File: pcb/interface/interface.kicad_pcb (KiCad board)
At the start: 2 copper layers, 45.8 x 24.8 mm, 15 parts, among them J1 SEGMENTS, J16 BUS_IN, J17 BUS_OUT, J5 SELECT, Q1 MMBT3904, Q2 MMBT3904, Q3 MMBT3904, Q4 MMBT3904, U1 74HC595, U2 74HC595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

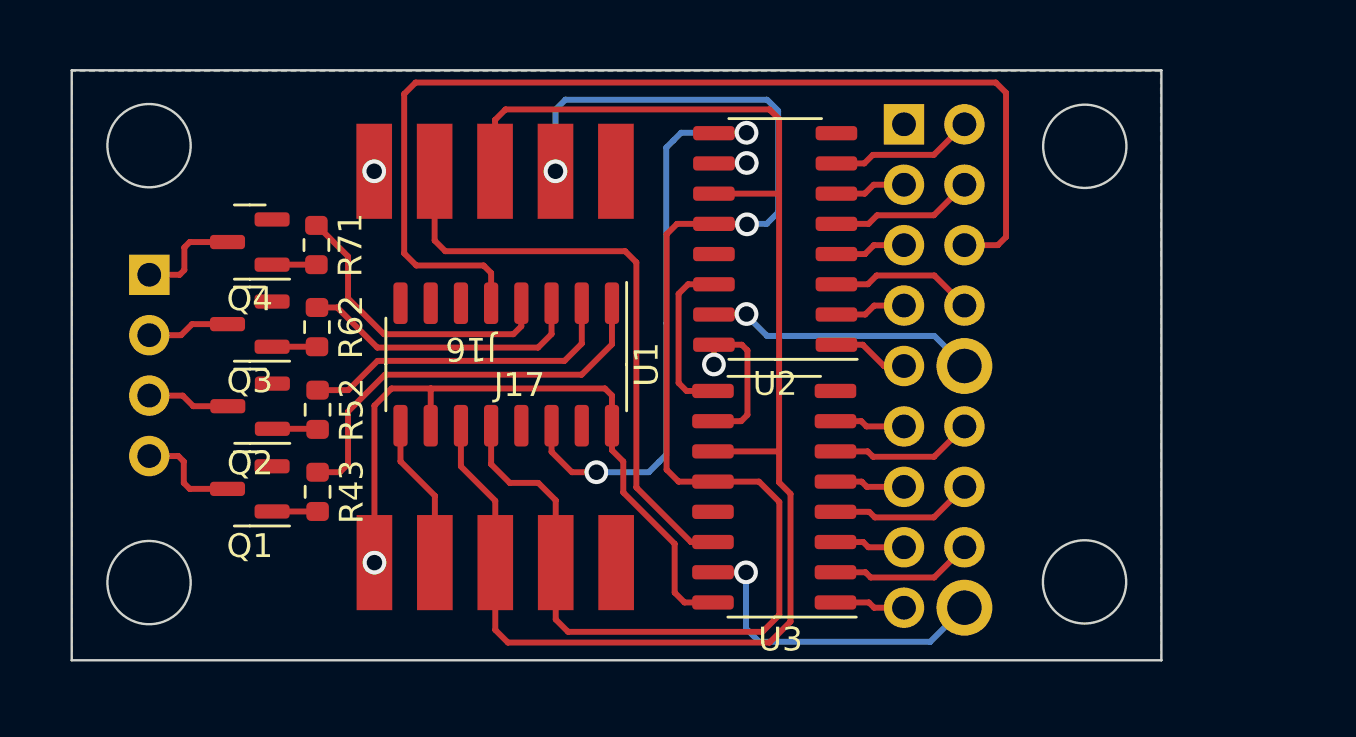
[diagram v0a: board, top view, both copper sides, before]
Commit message: cleaned up, reworked and (so far) finalized the interface board
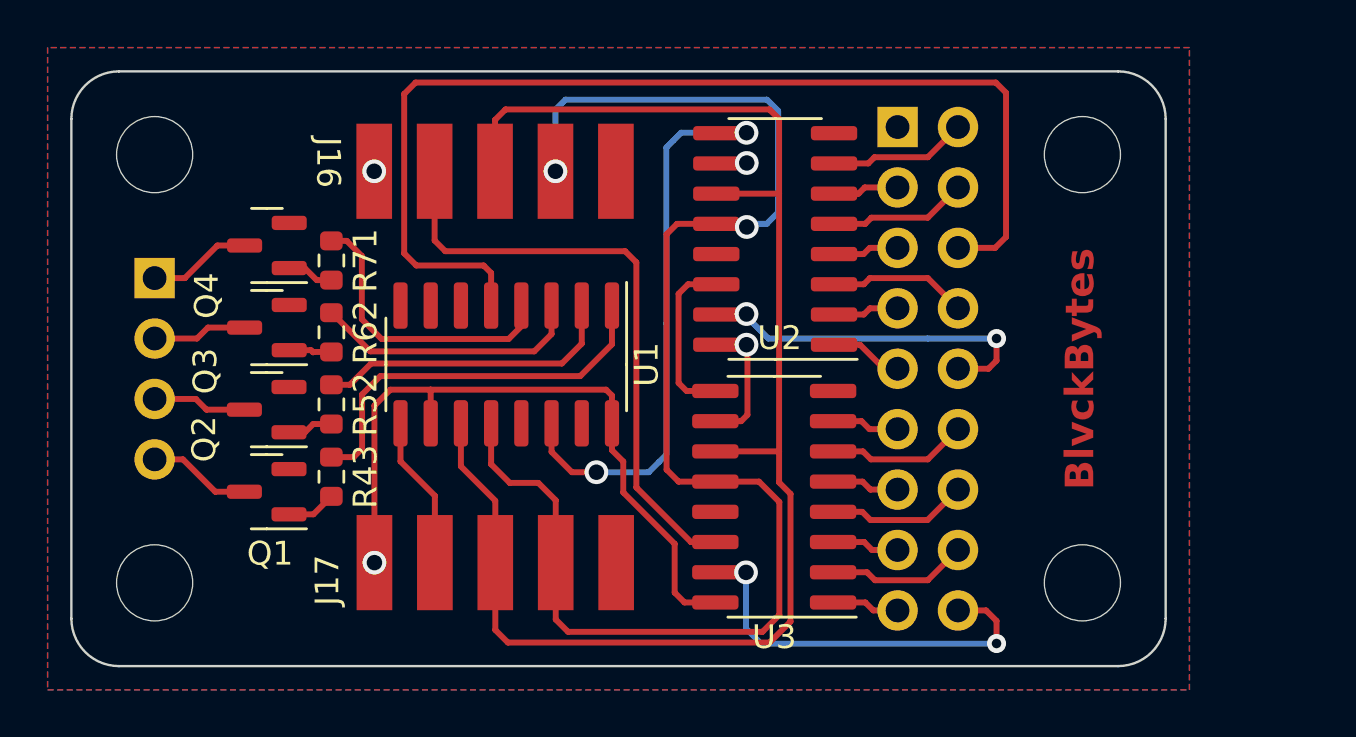
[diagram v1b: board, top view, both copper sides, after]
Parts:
- added REF**: MountingHole_3.2mm_M3, MountingHole:MountingHole_3.2mm_M3, F.Cu at (154.5, 102.0)
- added REF**: MountingHole_3.2mm_M3, MountingHole:MountingHole_3.2mm_M3, F.Cu at (115.5, 120.0)
- added REF**: MountingHole_3.2mm_M3, MountingHole:MountingHole_3.2mm_M3, F.Cu at (154.5, 120.0)
- added REF**: MountingHole_3.2mm_M3, MountingHole:MountingHole_3.2mm_M3, F.Cu at (115.5, 102.0)
- U1, U2, U3: footprint Package_SO:SO-16_3.9x9.9mm_P1.27mm -> Package_SO:SOIC-16_3.9x9.9mm_P1.27mm
- moved R71 0.91 mm to (122.9, 106.5)
- moved R43 0.86 mm to (122.9, 115.5)
- moved Q3 0.73 mm to (120.2, 109.3)
- moved Q4 0.73 mm to (120.2, 105.8)
- moved Q1 0.72 mm to (120.2, 116.2)
- moved Q2 0.71 mm to (120.2, 112.7)
- moved R62 0.64 mm to (122.9, 109.5)
- moved R52 0.62 mm to (122.9, 112.5)
- moved J1 0.29 mm to (146.7, 100.8)
- moved J5 0.26 mm to (115.5, 107.2)
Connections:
- net DBD_DISPLAY1_GND renamed DISPLAY1_GND
- net DBD_DISPLAY2_GND renamed DISPLAY2_GND
- net DBD_DISPLAY3_GND renamed DISPLAY3_GND
- net DBD_DISPLAY4_GND renamed DISPLAY4_GND
- U1 pad 5: DBD_DP -> DP
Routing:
- net DP: track 0.00 -> 45.9 mm
- net DBD_DP: track 45.6 -> 0.00 mm
- net M: track 11.5 -> 15.1 mm, vias 1 -> 2
- net B: track 14.1 -> 17.4 mm, vias 1 -> 2
- net +5V: track 37.7 -> 36.8 mm
- net Net-(U1-QB): track 17.6 -> 16.8 mm
- net Net-(U1-QC): track 13.6 -> 12.9 mm
- net Net-(U1-QD): track 12.1 -> 11.5 mm
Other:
- board size 45.8 x 24.8 mm -> 46 x 25 mm
- board text added: "BlvckBytes"

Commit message: added missing resistors to the interface board
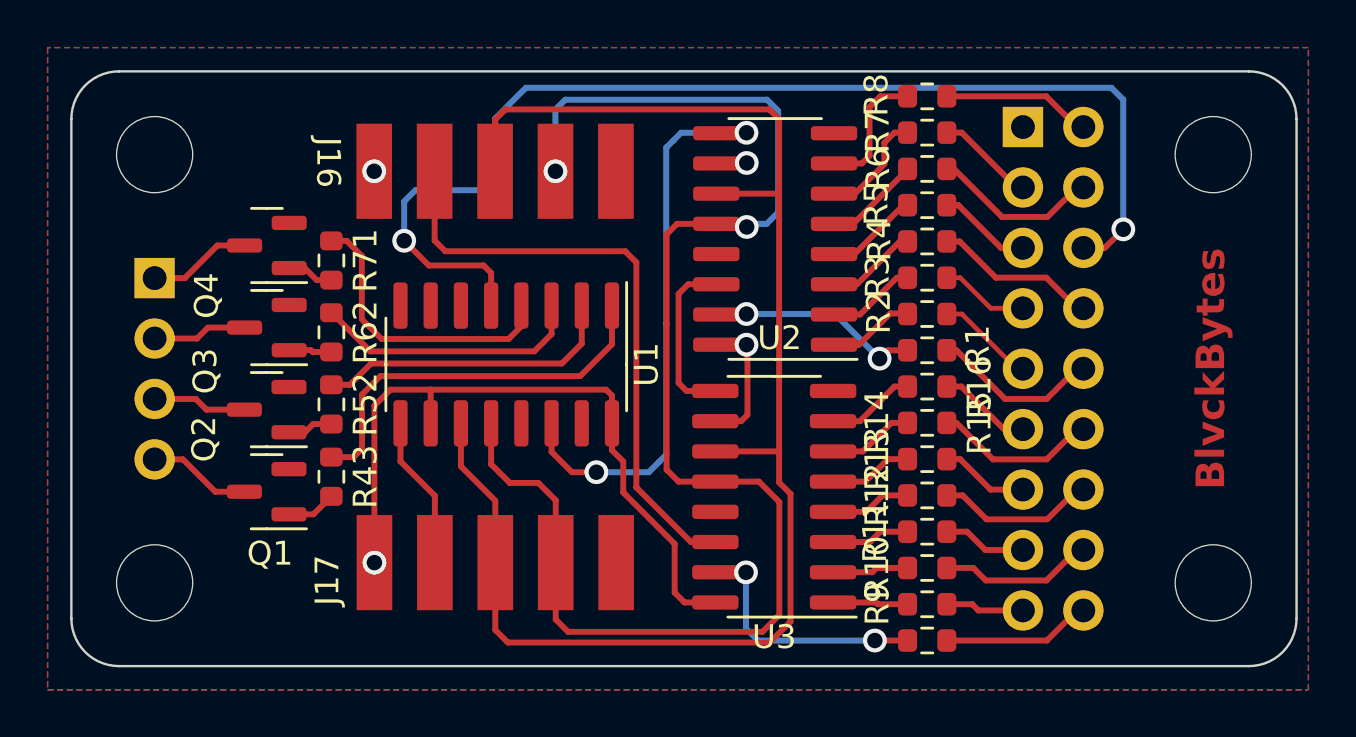
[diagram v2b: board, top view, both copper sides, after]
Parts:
- added R1: 220R, Resistor_SMD:R_0603_1608Metric, F.Cu at (148.0, 110.2)
- added R10: 220R, Resistor_SMD:R_0603_1608Metric, F.Cu at (148.0, 120.9)
- added R11: 220R, Resistor_SMD:R_0603_1608Metric, F.Cu at (148.0, 119.4)
- added R12: 220R, Resistor_SMD:R_0603_1608Metric, F.Cu at (148.0, 117.8)
- added R13: 220R, Resistor_SMD:R_0603_1608Metric, F.Cu at (148.0, 116.3)
- added R14: 220R, Resistor_SMD:R_0603_1608Metric, F.Cu at (148.0, 114.8)
- added R15: 220R, Resistor_SMD:R_0603_1608Metric, F.Cu at (148.0, 113.3)
- added R16: 220R, Resistor_SMD:R_0603_1608Metric, F.Cu at (148.0, 111.8)
- added R17: 220R, Resistor_SMD:R_0603_1608Metric, B.Cu at (129.8, 102.7)
- added R2: 220R, Resistor_SMD:R_0603_1608Metric, F.Cu at (148.0, 108.7)
- added R3: 220R, Resistor_SMD:R_0603_1608Metric, F.Cu at (148.0, 107.2)
- added R4: 220R, Resistor_SMD:R_0603_1608Metric, F.Cu at (148.0, 105.7)
- added R5: 220R, Resistor_SMD:R_0603_1608Metric, F.Cu at (148.0, 104.1)
- added R6: 220R, Resistor_SMD:R_0603_1608Metric, F.Cu at (148.0, 102.6)
- added R7: 220R, Resistor_SMD:R_0603_1608Metric, F.Cu at (148.0, 101.1)
- added R8: 220R, Resistor_SMD:R_0603_1608Metric, F.Cu at (148.0, 99.5)
- added R9: 220R, Resistor_SMD:R_0603_1608Metric, F.Cu at (148.0, 122.4)
- moved REF** 18.8 mm to (160.0, 120.0)
- moved REF** 18.8 mm to (160.0, 102.0)
- moved J1 5.27 mm to (152.0, 100.8)
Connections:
- U1 pad 5: DP -> Net-(U1-QF)
- U2 pad 1: P -> Net-(U2-QB)
- U2 pad 15: M -> Net-(U2-QA)
- U2 pad 2: N -> Net-(U2-QC)
- U2 pad 3: D -> Net-(U2-QD)
- U2 pad 4: O -> Net-(U2-QE)
- U2 pad 5: E -> Net-(U2-QF)
- U2 pad 6: G -> Net-(U2-QG)
- U2 pad 7: F -> Net-(U2-QH)
- U3 pad 1: A -> Net-(U3-QB)
- U3 pad 15: B -> Net-(U3-QA)
- U3 pad 2: K -> Net-(U3-QC)
- U3 pad 3: J -> Net-(U3-QD)
- U3 pad 4: C -> Net-(U3-QE)
- U3 pad 5: I -> Net-(U3-QF)
- U3 pad 6: L -> Net-(U3-QG)
- U3 pad 7: H -> Net-(U3-QH)
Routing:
- net B: track 17.4 -> 5.99 mm, vias 2 -> 0
- net Net-(U1-QF): track 0.00 -> 11.2 mm, vias 0 -> 1
- net Net-(U3-QA): track 0.00 -> 11.0 mm, vias 0 -> 2
- net DP: track 45.9 -> 36.2 mm, vias 0 -> 1
- net Net-(U2-QA): track 0.00 -> 9.12 mm, vias 0 -> 2
- net M: track 15.1 -> 6.84 mm, vias 2 -> 0
- net Net-(U2-QH): track 0.00 -> 5.46 mm
- net Net-(U2-QG): track 0.00 -> 4.68 mm
- net Net-(U2-QF): track 0.00 -> 4.06 mm
- net Net-(U2-QE): track 0.00 -> 3.94 mm
- net Net-(U2-QD): track 0.00 -> 3.84 mm
- net Net-(U3-QH): track 0.00 -> 3.73 mm
- net Net-(U2-QC): track 0.00 -> 3.73 mm
- net Net-(U2-QB): track 0.00 -> 3.65 mm
- net Net-(U3-QG): track 0.00 -> 3.63 mm
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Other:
- board size 46 x 25 mm -> 51.5 x 25 mm
